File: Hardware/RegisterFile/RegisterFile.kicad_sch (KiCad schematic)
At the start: 13 parts, among them J1 Conn_02x08_Odd_Even, J2 Conn_02x08_Odd_Even, J3 Conn_02x08_Odd_Even, J4 Conn_02x08_Odd_Even

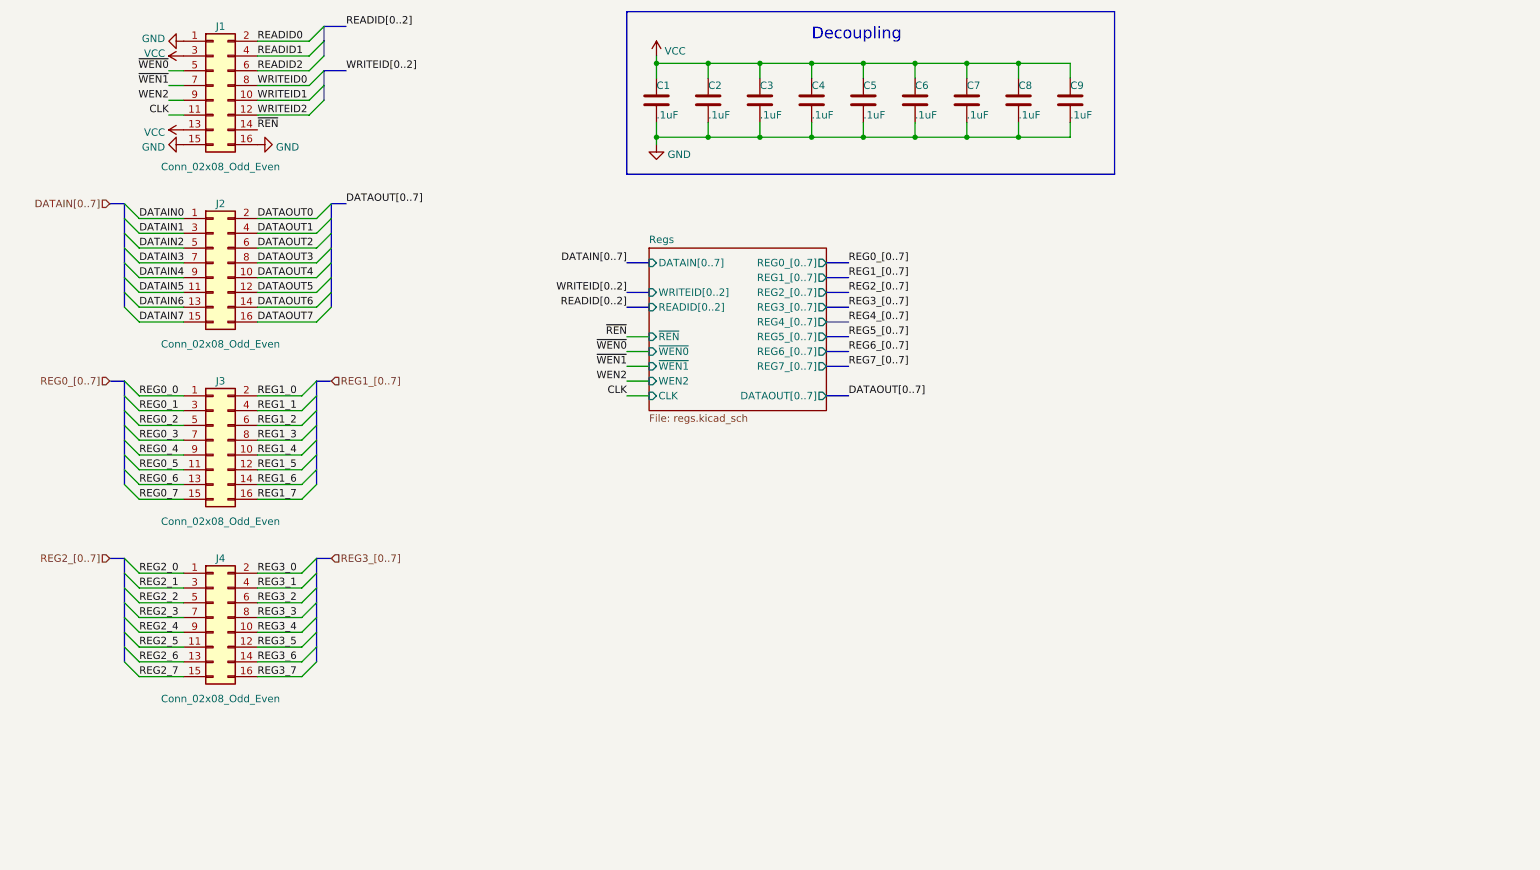
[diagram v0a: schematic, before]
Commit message: RegisterFile Layout: Everything except the "spider" (routing the all 8 muxes each to all 8 registers might be non-trivial)
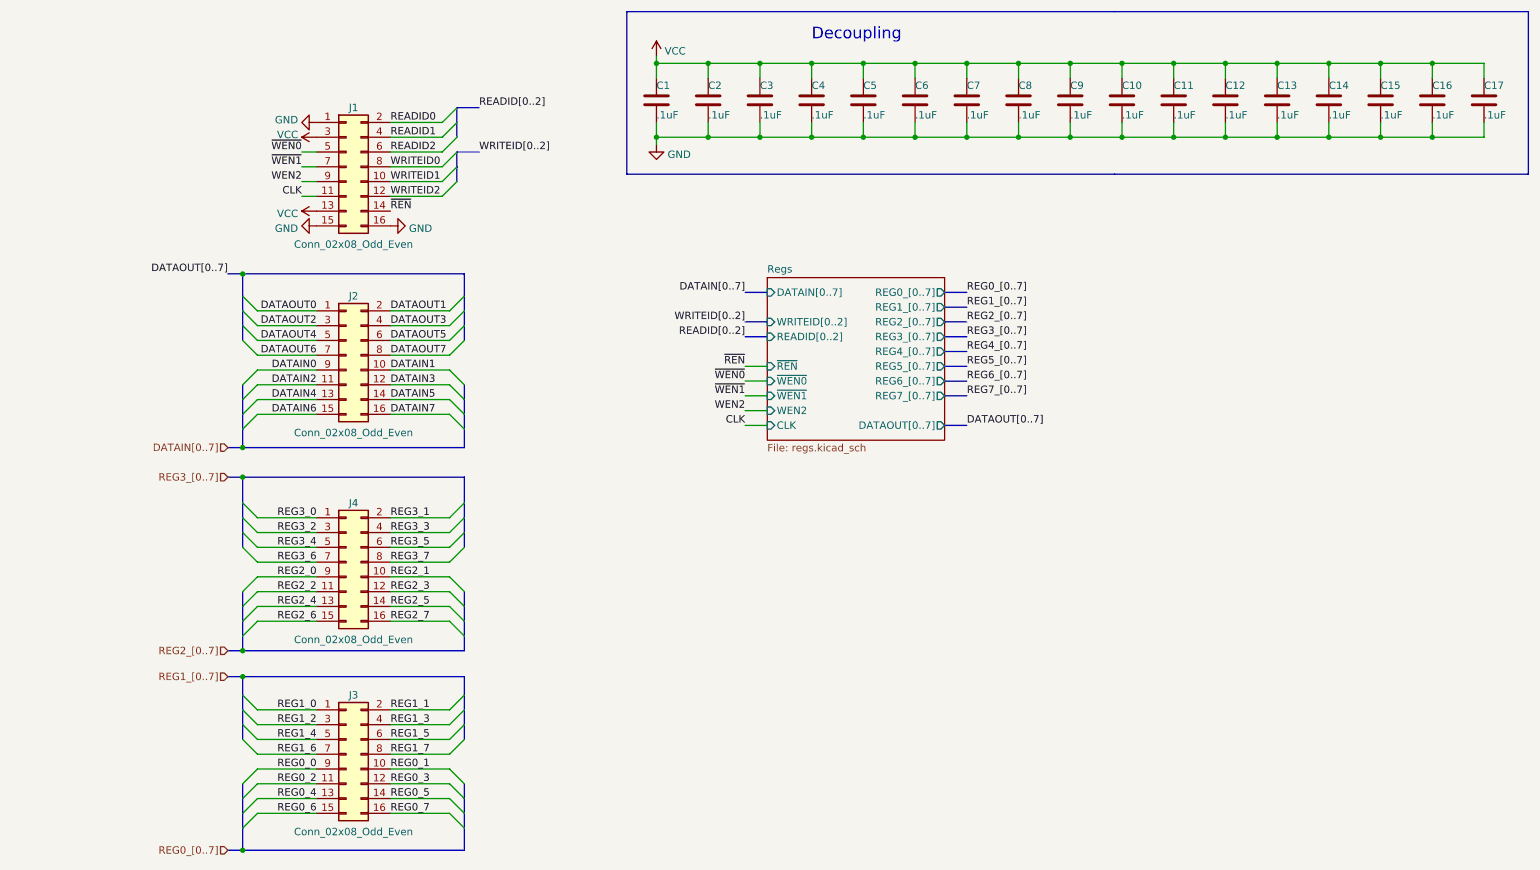
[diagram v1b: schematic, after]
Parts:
- added C10, C11, C12, C13, C14, C15, C16, C17: .1uF, Capacitor_SMD:C_1206_3216Metric_Pad1.33x1.80mm_HandSolder, symbol Device:C
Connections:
- net DATAIN0: now also J2.9 (Pin_9); no longer J2.1 (Pin_1)
- net DATAIN1: now also J2.10 (Pin_10); no longer J2.3 (Pin_3)
- net DATAIN2: now also J2.11 (Pin_11); no longer J2.5 (Pin_5)
- net DATAIN3: now also J2.12 (Pin_12); no longer J2.7 (Pin_7)
- net DATAIN4: now also J2.13 (Pin_13); no longer J2.9 (Pin_9)
- net DATAIN5: now also J2.14 (Pin_14); no longer J2.11 (Pin_11)
- net DATAIN6: now also J2.15 (Pin_15); no longer J2.13 (Pin_13)
- net DATAIN7: now also J2.16 (Pin_16); no longer J2.15 (Pin_15)
- net DATAOUT0: now also J2.1 (Pin_1); no longer J2.2 (Pin_2)
- net DATAOUT1: now also J2.2 (Pin_2); no longer J2.4 (Pin_4)
- net DATAOUT2: now also J2.3 (Pin_3); no longer J2.6 (Pin_6)
- net DATAOUT3: now also J2.4 (Pin_4); no longer J2.8 (Pin_8)
- net DATAOUT4: now also J2.5 (Pin_5); no longer J2.10 (Pin_10)
- net DATAOUT5: now also J2.6 (Pin_6); no longer J2.12 (Pin_12)
- net DATAOUT6: now also J2.7 (Pin_7); no longer J2.14 (Pin_14)
- net DATAOUT7: now also J2.8 (Pin_8); no longer J2.16 (Pin_16)
- net GND: now also C10.2, C11.2, C12.2, C13.2, C14.2, C15.2, C16.2, C17.2
- net REG0_0: now also J3.9 (Pin_9); no longer J3.1 (Pin_1)
- net REG0_1: now also J3.10 (Pin_10); no longer J3.3 (Pin_3)
- net REG0_2: now also J3.11 (Pin_11); no longer J3.5 (Pin_5)
- net REG0_3: now also J3.12 (Pin_12); no longer J3.7 (Pin_7)
- net REG0_4: now also J3.13 (Pin_13); no longer J3.9 (Pin_9)
- net REG0_5: now also J3.14 (Pin_14); no longer J3.11 (Pin_11)
- net REG0_6: now also J3.15 (Pin_15); no longer J3.13 (Pin_13)
- net REG0_7: now also J3.16 (Pin_16); no longer J3.15 (Pin_15)
- net REG1_0: now also J3.1 (Pin_1); no longer J3.2 (Pin_2)
- net REG1_1: now also J3.2 (Pin_2); no longer J3.4 (Pin_4)
- net REG1_2: now also J3.3 (Pin_3); no longer J3.6 (Pin_6)
- net REG1_3: now also J3.4 (Pin_4); no longer J3.8 (Pin_8)
- net REG1_4: now also J3.5 (Pin_5); no longer J3.10 (Pin_10)
- net REG1_5: now also J3.6 (Pin_6); no longer J3.12 (Pin_12)
- net REG1_6: now also J3.7 (Pin_7); no longer J3.14 (Pin_14)
- net REG1_7: now also J3.8 (Pin_8); no longer J3.16 (Pin_16)
- net REG2_0: now also J4.9 (Pin_9); no longer J4.1 (Pin_1)
- net REG2_1: now also J4.10 (Pin_10); no longer J4.3 (Pin_3)
- net REG2_2: now also J4.11 (Pin_11); no longer J4.5 (Pin_5)
- net REG2_3: now also J4.12 (Pin_12); no longer J4.7 (Pin_7)
- net REG2_4: now also J4.13 (Pin_13); no longer J4.9 (Pin_9)
- net REG2_5: now also J4.14 (Pin_14); no longer J4.11 (Pin_11)
- net REG2_6: now also J4.15 (Pin_15); no longer J4.13 (Pin_13)
- net REG2_7: now also J4.16 (Pin_16); no longer J4.15 (Pin_15)
- net REG3_0: now also J4.1 (Pin_1); no longer J4.2 (Pin_2)
- net REG3_1: now also J4.2 (Pin_2); no longer J4.4 (Pin_4)
- net REG3_2: now also J4.3 (Pin_3); no longer J4.6 (Pin_6)
- net REG3_3: now also J4.4 (Pin_4); no longer J4.8 (Pin_8)
- net REG3_4: now also J4.5 (Pin_5); no longer J4.10 (Pin_10)
- net REG3_5: now also J4.6 (Pin_6); no longer J4.12 (Pin_12)
- net REG3_6: now also J4.7 (Pin_7); no longer J4.14 (Pin_14)
- net REG3_7: now also J4.8 (Pin_8); no longer J4.16 (Pin_16)
- net VCC: now also C10.1, C11.1, C12.1, C13.1, C14.1, C15.1, C16.1, C17.1
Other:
- moved on the sheet: J1, J2, J3, J4
